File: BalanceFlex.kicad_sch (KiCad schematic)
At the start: 9 parts, among them J1 Conn_01x10_Socket, J2 Conn_01x02_Socket, J3 Conn_01x01, J4 Conn_01x01, J5 Conn_01x01, J6 Conn_01x01, J7 Conn_01x01, J8 Conn_01x01, J9 Conn_01x01

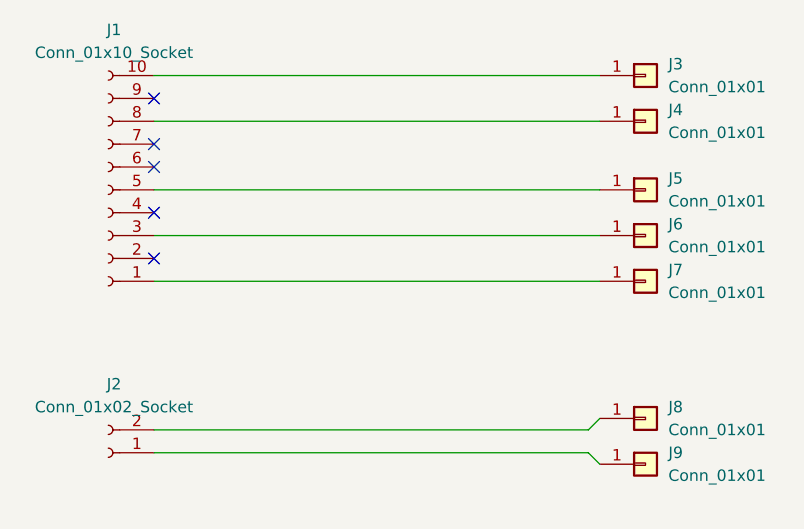
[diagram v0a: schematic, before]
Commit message: Cleaning up layout and adding in thermistors
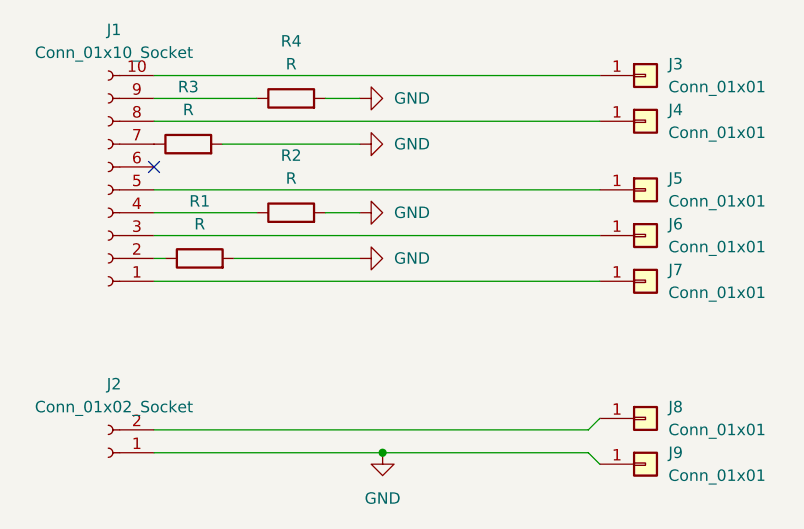
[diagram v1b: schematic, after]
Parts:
- added R1, R2, R3, R4: R, Resistor_SMD:R_0402_1005Metric, symbol Device:R
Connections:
- net at J1.2 (Pin_2): now also R1.1
- net at J1.4 (Pin_4): now also R2.1
- net at J1.7 (Pin_7): now also R3.1
- net at J1.9 (Pin_9): now also R4.1
- net GND: now reaches J2.1 (Pin_1), J9.1 (Pin_1)
- net GND: now also R1.2, R2.2, R3.2, R4.2
- no-connect marks 5 -> 1

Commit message: had to add all files because I download zip instead of cloned
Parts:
- removed R1, R2, R3, R4: R, Resistor_SMD:R_0402_1005Metric, symbol Device:R
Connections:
- net at J1.1 (Pin_1), J7.1 (Pin_1): now also J1.2 (Pin_2)
- net at J1.10 (Pin_10), J3.1 (Pin_1): now also J1.9 (Pin_9)
- net at J1.3 (Pin_3), J6.1 (Pin_1): now also J1.4 (Pin_4)
- net at J1.5 (Pin_5), J5.1 (Pin_1): now also J1.6 (Pin_6)
- net at J1.7 (Pin_7): now also J1.8 (Pin_8), J4.1 (Pin_1)
- no-connect marks 1 -> 0
